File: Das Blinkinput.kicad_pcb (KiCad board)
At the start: 2 copper layers, 50.8 x 12.7 mm, 0 parts

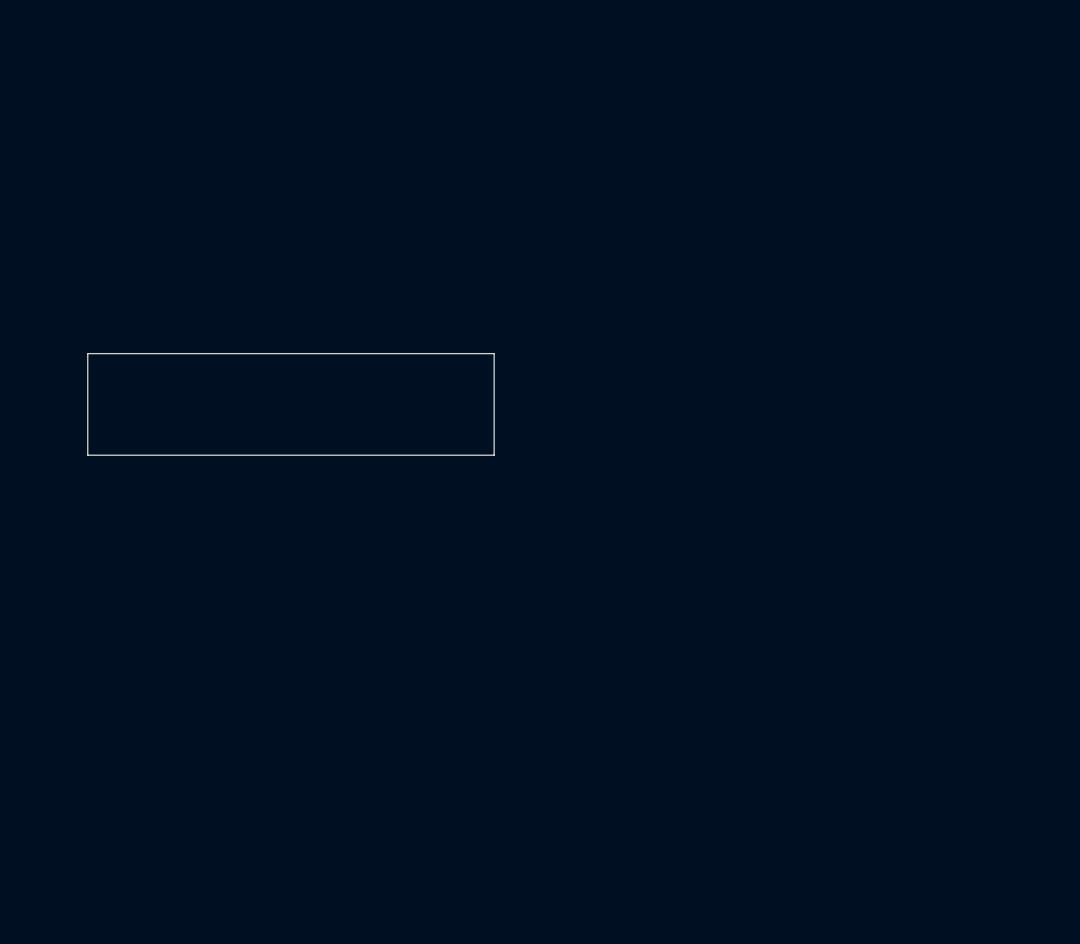
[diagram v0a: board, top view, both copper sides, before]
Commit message: Added libraries and imported components into the layout
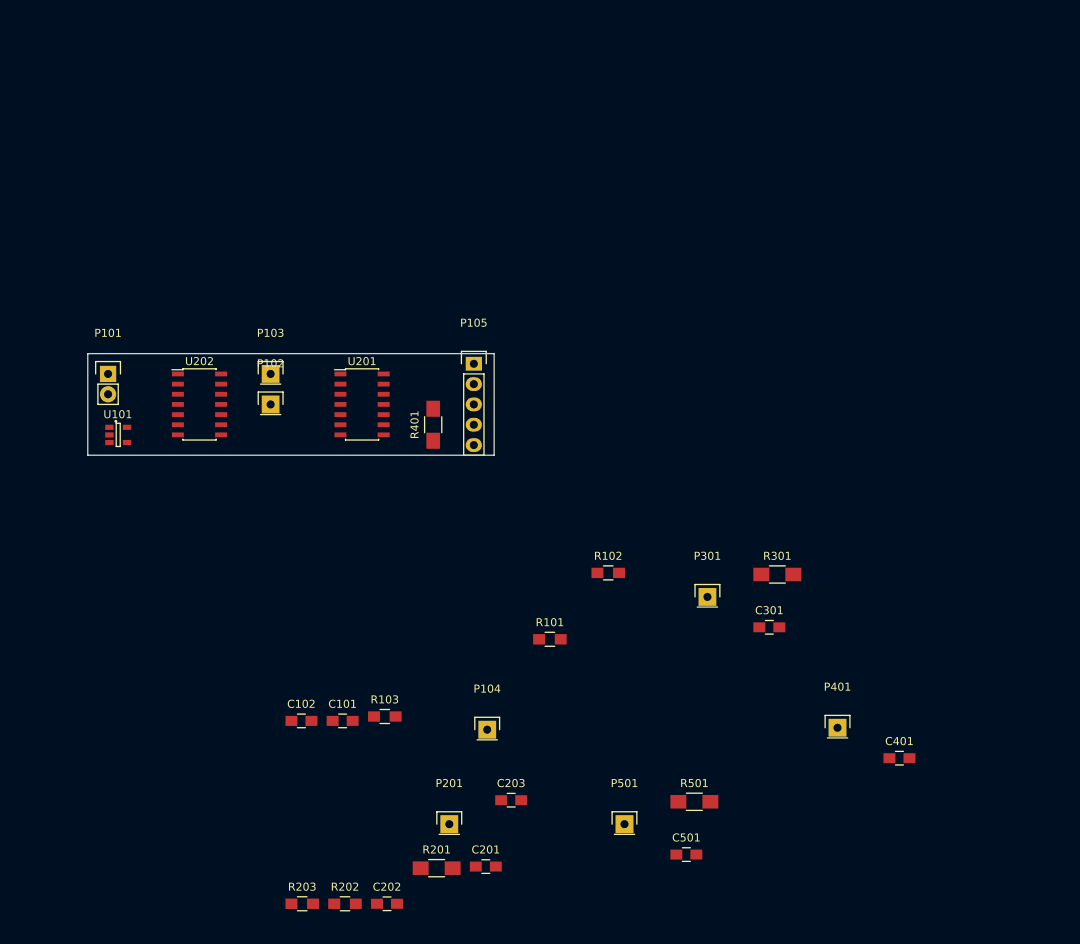
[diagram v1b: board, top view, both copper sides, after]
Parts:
- added C101: 1U, Capacitors_SMD:C_0805_HandSoldering, F.Cu at (109.3, 151.3)
- added C102: 1U, Capacitors_SMD:C_0805_HandSoldering, F.Cu at (104.2, 151.3)
- added C201: .1U, Capacitors_SMD:C_0805_HandSoldering, F.Cu at (127.2, 169.5)
- added C202: 100p, Capacitors_SMD:C_0805_HandSoldering, F.Cu at (114.9, 174.2)
- added C203: .1U, Capacitors_SMD:C_0805_HandSoldering, F.Cu at (130.4, 161.2)
- added C301: 100p, Capacitors_SMD:C_0805_HandSoldering, F.Cu at (162.7, 139.6)
- added C401: 100p, Capacitors_SMD:C_0805_HandSoldering, F.Cu at (178.9, 156.0)
- added C501: 100p, Capacitors_SMD:C_0805_HandSoldering, F.Cu at (152.3, 168.0)
- added P101: CONN_01X02, Pin_Headers:Pin_Header_Straight_1x02, F.Cu at (80.0, 108.0)
- added P102: CONN_01X01, Pin_Headers:Pin_Header_Straight_1x01, F.Cu at (100.3, 111.8)
- added P103: CONN_01X01, Pin_Headers:Pin_Header_Straight_1x01, F.Cu at (100.3, 108.0)
- added P104: CONN_01X01, Pin_Headers:Pin_Header_Straight_1x01, F.Cu at (127.4, 152.4)
- added P105: CONN_01X05, Pin_Headers:Pin_Header_Straight_1x05, F.Cu at (125.7, 106.7)
- added P201: CONN_01X01, Pin_Headers:Pin_Header_Straight_1x01, F.Cu at (122.7, 164.2)
- added P301: CONN_01X01, Pin_Headers:Pin_Header_Straight_1x01, F.Cu at (154.9, 135.8)
- added P401: CONN_01X01, Pin_Headers:Pin_Header_Straight_1x01, F.Cu at (171.2, 152.2)
- added P501: CONN_01X01, Pin_Headers:Pin_Header_Straight_1x01, F.Cu at (144.6, 164.2)
- added R101: 0, Resistors_SMD:R_0805_HandSoldering, F.Cu at (135.2, 141.1)
- added R102: 10K, Resistors_SMD:R_0805_HandSoldering, F.Cu at (142.5, 132.8)
- added R103: 10K, Resistors_SMD:R_0805_HandSoldering, F.Cu at (114.6, 150.8)
- added R201: 1MEG, Resistors_SMD:R_1206_HandSoldering, F.Cu at (121.1, 169.7)
- added R202: 10K, Resistors_SMD:R_0805_HandSoldering, F.Cu at (109.6, 174.2)
- added R203: 10K, Resistors_SMD:R_0805_HandSoldering, F.Cu at (104.3, 174.2)
- added R301: 1MEG, Resistors_SMD:R_1206_HandSoldering, F.Cu at (163.7, 133.0)
- added R401: 1MEG, Resistors_SMD:R_1206_HandSoldering, F.Cu at (120.7, 114.3)
- added R501: 1MEG, Resistors_SMD:R_1206_HandSoldering, F.Cu at (153.3, 161.4)
- added U101: LP2980IM5-3.0/NOPB, Housings_SOT-23_SOT-143_TSOT-6:SOT-23-5, F.Cu at (81.3, 115.6)
- added U201: MCP6404, Housings_SOIC:SOIC-14_3.9x8.7mm_Pitch1.27mm, F.Cu at (111.8, 111.8)
- added U202: LM339, Housings_SOIC:SOIC-14_3.9x8.7mm_Pitch1.27mm, F.Cu at (91.4, 111.8)

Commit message: Added photodiode component to new local footprint library
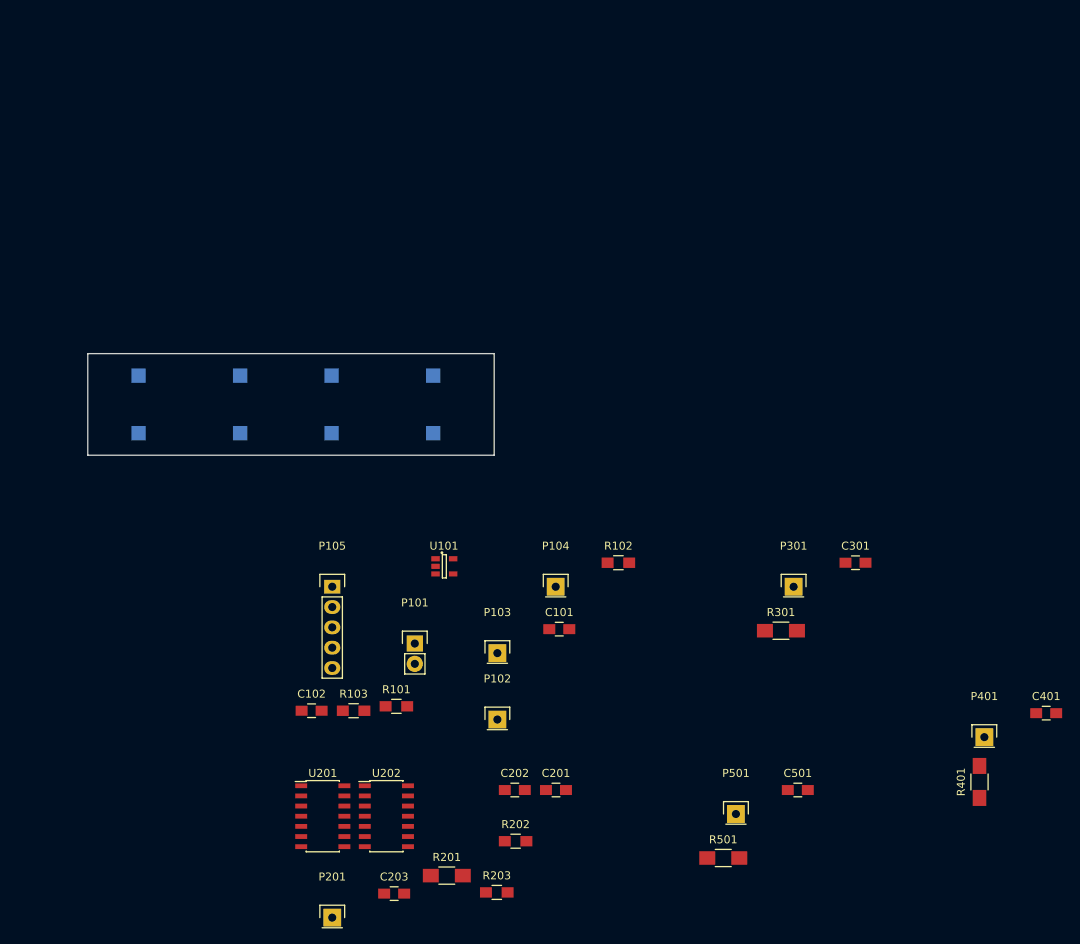
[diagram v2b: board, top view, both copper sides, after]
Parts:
- added PD201: VBPW34SR, DasBlinkinput:VPW34SR, B.Cu at (83.8, 111.8)
- added PD301: VBPW34SR, DasBlinkinput:VPW34SR, B.Cu at (108.0, 111.8)
- added PD401: VBPW34SR, DasBlinkinput:VPW34SR, B.Cu at (120.7, 111.8)
- added PD501: VBPW34SR, DasBlinkinput:VPW34SR, B.Cu at (96.5, 111.8)
- moved R401 81.6 mm to (188.9, 158.9)
- moved U202 56.5 mm to (114.8, 163.2)
- moved U201 51.7 mm to (106.8, 163.2)
- moved P101 51.0 mm to (118.4, 141.6)
- moved P102 48.5 mm to (128.7, 151.1)
- moved P103 45.0 mm to (128.7, 142.8)
- moved U101 44.0 mm to (122.0, 132.0)
- moved P105 33.0 mm to (108.0, 134.5)
- moved C101 29.4 mm to (136.4, 139.8)
- moved R203 24.4 mm to (128.6, 172.8)
- moved R202 22.7 mm to (130.9, 166.4)
- moved C202 21.4 mm to (130.8, 160.0)
- moved R101 20.9 mm to (116.0, 149.5)
- moved P104 19.8 mm to (136.0, 134.5)
- moved C401 19.2 mm to (197.3, 150.3)
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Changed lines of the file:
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@@
 (kicad_pcb (version 4) (host pcbnew 0.201505141916+5653~23~ubuntu14.04.1-product)
   (general
-    (links 61)
-    (no_connects 61)
-    (area 77.419999 105.359999 128.320001 118.160001)
+    (links 69)
+    (no_connects 69)
+    (area 76.099999 65.939999 199.858002 177.938001)
     (thickness 1.6)
     (drawings 8)
     (tracks 0)
     (zones 0)
-    (modules 29)
+    (modules 33)
     (nets 21)
   )
@@
   )
   (module Capacitors_SMD:C_0805_HandSoldering (layer F.Cu)
-    (at 109.329001 151.319)
+    (at 136.409001 139.849)
     (descr "Capacitor SMD 0805, hand soldering")
     (tags "capacitor 0805")
@@
   )
   (module Capacitors_SMD:C_0805_HandSoldering (layer F.Cu)
-    (at 104.179001 151.319)
+    (at 105.449001 150.049)
     (descr "Capacitor SMD 0805, hand soldering")
     (tags "capacitor 0805")
@@
   )
   (module Capacitors_SMD:C_0805_HandSoldering (layer F.Cu)
-    (at 127.229001 169.529)
+    (at 135.999001 159.959)
     (descr "Capacitor SMD 0805, hand soldering")
     (tags "capacitor 0805")
@@
   )
   (module Capacitors_SMD:C_0805_HandSoldering (layer F.Cu)
-    (at 114.879001 174.179)
+    (at 130.849001 159.959)
     (descr "Capacitor SMD 0805, hand soldering")
     (tags "capacitor 0805")
@@
   )
   (module Capacitors_SMD:C_0805_HandSoldering (layer F.Cu)
-    (at 130.399001 161.229)
+    (at 115.769001 172.909)
     (descr "Capacitor SMD 0805, hand soldering")
     (tags "capacitor 0805")
@@
   )
   (module Capacitors_SMD:C_0805_HandSoldering (layer F.Cu)
-    (at 162.669001 139.619)
+    (at 173.439001 131.549)
     (descr "Capacitor SMD 0805, hand soldering")
     (tags "capacitor 0805")
@@
   )
   (module Capacitors_SMD:C_0805_HandSoldering (layer F.Cu)
-    (at 178.929001 155.979)
+    (at 197.279001 150.349)
     (descr "Capacitor SMD 0805, hand soldering")
     (tags "capacitor 0805")
@@
   )
   (module Capacitors_SMD:C_0805_HandSoldering (layer F.Cu)
-    (at 152.299001 168.029)
+    (at 166.229001 159.959)
     (descr "Capacitor SMD 0805, hand soldering")
     (tags "capacitor 0805")
@@
   )
   (module Pin_Headers:Pin_Header_Straight_1x02 (layer F.Cu)
-    (at 80.01 107.95)
+    (at 118.352333 141.649)
     (descr "Through hole pin header")
     (tags "pin header")
@@
   )
   (module Pin_Headers:Pin_Header_Straight_1x01 (layer F.Cu)
-    (at 100.33 111.76)
+    (at 128.672333 151.149)
     (descr "Through hole pin header")
     (tags "pin header")
@@
   )
   (module Pin_Headers:Pin_Header_Straight_1x01 (layer F.Cu)
-    (at 100.33 107.95)
+    (at 128.672333 142.849)
     (descr "Through hole pin header")
     (tags "pin header")
@@
   )
   (module Pin_Headers:Pin_Header_Straight_1x01 (layer F.Cu)
-    (at 127.402333 152.419)
+    (at 135.962333 134.549)
     (descr "Through hole pin header")
     (tags "pin header")
@@
   )
   (module Pin_Headers:Pin_Header_Straight_1x05 (layer F.Cu)
-    (at 125.73 106.68)
+    (at 108.032333 134.549)
     (descr "Through hole pin header")
     (tags "pin header")
@@
   )
   (module Pin_Headers:Pin_Header_Straight_1x01 (layer F.Cu)
-    (at 122.662333 164.229)
+    (at 108.032333 175.909)
     (descr "Through hole pin header")
     (tags "pin header")
@@
   )
   (module Pin_Headers:Pin_Header_Straight_1x01 (layer F.Cu)
-    (at 154.932333 135.819)
+    (at 165.702333 134.549)
     (descr "Through hole pin header")
     (tags "pin header")
@@
   )
   (module Pin_Headers:Pin_Header_Straight_1x01 (layer F.Cu)
-    (at 171.192333 152.179)
+    (at 189.542333 153.349)
     (descr "Through hole pin header")
     (tags "pin header")
@@
   )
   (module Pin_Headers:Pin_Header_Straight_1x01 (layer F.Cu)
-    (at 144.562333 164.229)
+    (at 158.492333 162.959)
     (descr "Through hole pin header")
     (tags "pin header")
@@
   )
   (module Resistors_SMD:R_0805_HandSoldering (layer F.Cu)
-    (at 135.239001 141.119)
+    (at 116.049001 149.499)
     (descr "Resistor SMD 0805, hand soldering")
     (tags "resistor 0805")
@@
   )
   (module Resistors_SMD:R_0805_HandSoldering (layer F.Cu)
-    (at 142.529001 132.819)
+    (at 143.799001 131.549)
     (descr "Resistor SMD 0805, hand soldering")
     (tags "resistor 0805")
@@
   )
   (module Resistors_SMD:R_0805_HandSoldering (layer F.Cu)
-    (at 114.599001 150.769)
+    (at 110.699001 150.049)
     (descr "Resistor SMD 0805, hand soldering")
     (tags "resistor 0805")
@@
   )
   (module Resistors_SMD:R_1206_HandSoldering (layer F.Cu)
-    (at 121.079001 169.729)
+    (at 122.349001 170.659)
     (descr "Resistor SMD 1206, hand soldering")
     (tags "resistor 1206")
@@
   )
   (module Resistors_SMD:R_0805_HandSoldering (layer F.Cu)
-    (at 109.629001 174.179)
+    (at 130.949001 166.359)
     (descr "Resistor SMD 0805, hand soldering")
     (tags "resistor 0805")
@@
   )
   (module Resistors_SMD:R_0805_HandSoldering (layer F.Cu)
-    (at 104.279001 174.179)
+    (at 128.599001 172.759)
     (descr "Resistor SMD 0805, hand soldering")
     (tags "resistor 0805")
@@
   )
   (module Resistors_SMD:R_1206_HandSoldering (layer F.Cu)
-    (at 163.669001 133.019)
+    (at 164.119001 140.049)
     (descr "Resistor SMD 1206, hand soldering")
     (tags "resistor 1206")
@@
   )
   (module Resistors_SMD:R_1206_HandSoldering (layer F.Cu)
-    (at 120.65 114.3 90)
+    (at 188.937571 158.949001 90)
     (descr "Resistor SMD 1206, hand soldering")
     (tags "resistor 1206")
@@
   )
   (module Resistors_SMD:R_1206_HandSoldering (layer F.Cu)
-    (at 153.299001 161.429)
+    (at 156.909001 168.459)
     (descr "Resistor SMD 1206, hand soldering")
     (tags "resistor 1206")
@@
   )
   (module Housings_SOT-23_SOT-143_TSOT-6:SOT-23-5 (layer F.Cu)
-    (at 81.28 115.57)
+    (at 122.04519 131.999)
     (descr "5-pin SOT23 package")
     (tags SOT-23-5)
@@
   )
   (module Housings_SOIC:SOIC-14_3.9x8.7mm_Pitch1.27mm (layer F.Cu)
-    (at 111.76 111.76)
+    (at 106.849001 163.234)
     (descr "14-Lead Plastic Small Outline (SL) - Narrow, 3.90 mm Body [SOIC] (see Microchip Packaging Specification 00000049BS.pdf)")
     (tags "SOIC 1.27")
@@
   )
   (module Housings_SOIC:SOIC-14_3.9x8.7mm_Pitch1.27mm (layer F.Cu)
-    (at 91.44 111.76)
+    (at 114.799001 163.234)
     (descr "14-Lead Plastic Small Outline (SL) - Narrow, 3.90 mm Body [SOIC] (see Microchip Packaging Specification 00000049BS.pdf)")
     (tags "SOIC 1.27")
@@
     )
   )
+  (module DasBlinkinput:VPW34SR (layer B.Cu)
+    (at 83.82 111.76 90)
+    (fp_text reference PD201 (at 0 -3.5 90) (layer B.SilkS)
+      (effects (font (size 1 1) (thickness 0.15)) (justify mirror))
+    )
+    (fp_text value VBPW34SR (at -0.1 4.8 90) (layer B.Fab)
+      (effects (font (size 1 1) (thickness 0.15)) (justify mirror))
+    )
+    (fp_line (start -2 2.2) (end -2 -2.2) (layer B.SilkS) (width 0.15))
+    (fp_line (start -2 -2.2) (end 2 -2.2) (layer B.SilkS) (width 0.15))
+    (fp_line (start 2 2.2) (end 2 -2.2) (layer B.SilkS) (width 0.15))
+    (fp_line (start -2 2.2) (end 2 2.2) (layer B.SilkS) (width 0.15))
+    (pad 1 smd rect (at -3.6 0 90) (size 1.8 1.8) (layers B.Cu B.Paste B.Mask)
+      (net 12 VGND))
+    (pad 2 smd rect (at 3.6 0 90) (size 1.8 1.8) (layers B.Cu B.Paste B.Mask)
+      (net 5 "Net-(C202-Pad2)"))
+  )
+  (module DasBlinkinput:VPW34SR (layer B.Cu)
+    (at 107.95 111.76 90)
+    (fp_text reference PD301 (at 0 -3.5 90) (layer B.SilkS)
+      (effects (font (size 1 1) (thickness 0.15)) (justify mirror))
+    )
+    (fp_text value VBPW34SR (at -0.1 4.8 90) (layer B.Fab)
+      (effects (font (size 1 1) (thickness 0.15)) (justify mirror))
+    )
+    (fp_line (start -2 2.2) (end -2 -2.2) (layer B.SilkS) (width 0.15))
+    (fp_line (start -2 -2.2) (end 2 -2.2) (layer B.SilkS) (width 0.15))
+    (fp_line (start 2 2.2) (end 2 -2.2) (layer B.SilkS) (width 0.15))
+    (fp_line (start -2 2.2) (end 2 2.2) (layer B.SilkS) (width 0.15))
+    (pad 1 smd rect (at -3.6 0 90) (size 1.8 1.8) (layers B.Cu B.Paste B.Mask)
+      (net 12 VGND))
+    (pad 2 smd rect (at 3.6 0 90) (size 1.8 1.8) (layers B.Cu B.Paste B.Mask)
+      (net 7 "Net-(C301-Pad2)"))
+  )
+  (module DasBlinkinput:VPW34SR (layer B.Cu)
+    (at 120.65 111.76 90)
+    (fp_text reference PD401 (at 0 -3.5 90) (layer B.SilkS)
+      (effects (font (size 1 1) (thickness 0.15)) (justify mirror))
+    )
+    (fp_text value VBPW34SR (at -0.1 4.8 90) (layer B.Fab)
+      (effects (font (size 1 1) (thickness 0.15)) (justify mirror))
+    )
+    (fp_line (start -2 2.2) (end -2 -2.2) (layer B.SilkS) (width 0.15))
+    (fp_line (start -2 -2.2) (end 2 -2.2) (layer B.SilkS) (width 0.15))
+    (fp_line (start 2 2.2) (end 2 -2.2) (layer B.SilkS) (width 0.15))
+    (fp_line (start -2 2.2) (end 2 2.2) (layer B.SilkS) (width 0.15))
+    (pad 1 smd rect (at -3.6 0 90) (size 1.8 1.8) (layers B.Cu B.Paste B.Mask)
+      (net 12 VGND))
+    (pad 2 smd rect (at 3.6 0 90) (size 1.8 1.8) (layers B.Cu B.Paste B.Mask)
+      (net 9 "Net-(C401-Pad2)"))
+  )
+  (module DasBlinkinput:VPW34SR (layer B.Cu)
+    (at 96.52 111.76 90)
+    (fp_text reference PD501 (at 0 -3.5 90) (layer B.SilkS)
+      (effects (font (size 1 1) (thickness 0.15)) (justify mirror))
+    )
+    (fp_text value VBPW34SR (at -0.1 4.8 90) (layer B.Fab)
+      (effects (font (size 1 1) (thickness 0.15)) (justify mirror))
+    )
+    (fp_line (start -2 2.2) (end -2 -2.2) (layer B.SilkS) (width 0.15))
+    (fp_line (start -2 -2.2) (end 2 -2.2) (layer B.SilkS) (width 0.15))
+    (fp_line (start 2 2.2) (end 2 -2.2) (layer B.SilkS) (width 0.15))
+    (fp_line (start -2 2.2) (end 2 2.2) (layer B.SilkS) (width 0.15))
+    (pad 1 smd rect (at -3.6 0 90) (size 1.8 1.8) (layers B.Cu B.Paste B.Mask)
+      (net 12 VGND))
+    (pad 2 smd rect (at 3.6 0 90) (size 1.8 1.8) (layers B.Cu B.Paste B.Mask)
+      (net 11 "Net-(C501-Pad2)"))
+  )
   (gr_line (start 77.47 105.41) (end 77.47 118.11) (angle 90) (layer Edge.Cuts) (width 0.1))
